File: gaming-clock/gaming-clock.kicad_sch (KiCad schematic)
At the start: 24 parts, among them J1 USB_C_Receptacle_USB2.0, U1 ESP32-C3-WROOM-02, U2 LM1117GS-3.3

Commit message: newsheet
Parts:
- removed D10, D11, D12, D13, D14, D15, D2, D3, D4, D5, D6, D7, D8, D9: SK6812MINI, LED_SMD:LED_SK6812MINI_PLCC4_3.5x3.5mm_P1.75mm, symbol LED:SK6812MINI
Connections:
- net 7-Segment-ARGB/DIN: now reaches U1.18 (GPIO0/ADC1_CH0/XTAL_32K_P)
- net DIN1 renamed 7-Segment-ARGB1/DIN
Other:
- added sheet 7-Segment-ARGB (untitled.kicad_sch)
- added sheet 7-Segment-ARGB1 (untitled.kicad_sch)

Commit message: c
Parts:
- removed D1: DＧＳ１０１０ＦＬ, Diode_SMD:D_SOD-123F, symbol Device:D
- added C5: 10u, Capacitor_SMD:C_0603_1608Metric_Pad1.08x0.95mm_HandSolder, symbol Device:C
- added C6: 100n, Capacitor_SMD:C_0603_1608Metric_Pad1.08x0.95mm_HandSolder, symbol Device:C
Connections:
- net +3.3V: now also C5.1, C6.1; no longer U1.1 (3V3)
- net 7-Segment-ARGB/DIN: now also U1.3 (GPIO4/ADC1_CH4); no longer U1.18 (GPIO0/ADC1_CH0/XTAL_32K_P)
- net 7-Segment-ARGB1/DIN: now also U1.4 (GPIO5/ADC2_CH0); no longer U1.17 (GPIO1/ADC1_CH1/XTAL_32K_N)
- net D-: now reaches U1.13 (GPIO18/USB_D-)
- net D-: now also J1.A7 (D-), J1.B7 (D-)
- net D+: now reaches U1.14 (GPIO19/USB_D+)
- net D+: now also J1.A6 (D+), J1.B6 (D+)
- net 7-Segment-ARGB2/DIN: now reaches U1.5 (GPIO6)
- net 7-Segment-ARGB3/DIN: now reaches U1.6 (GPIO7)
- new net: C5.2, C6.2, U1.1 (3V3)
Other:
- added sheet 7-Segment-ARGB2 (untitled.kicad_sch)
- added sheet 7-Segment-ARGB3 (untitled.kicad_sch)
- moved on the sheet: U1

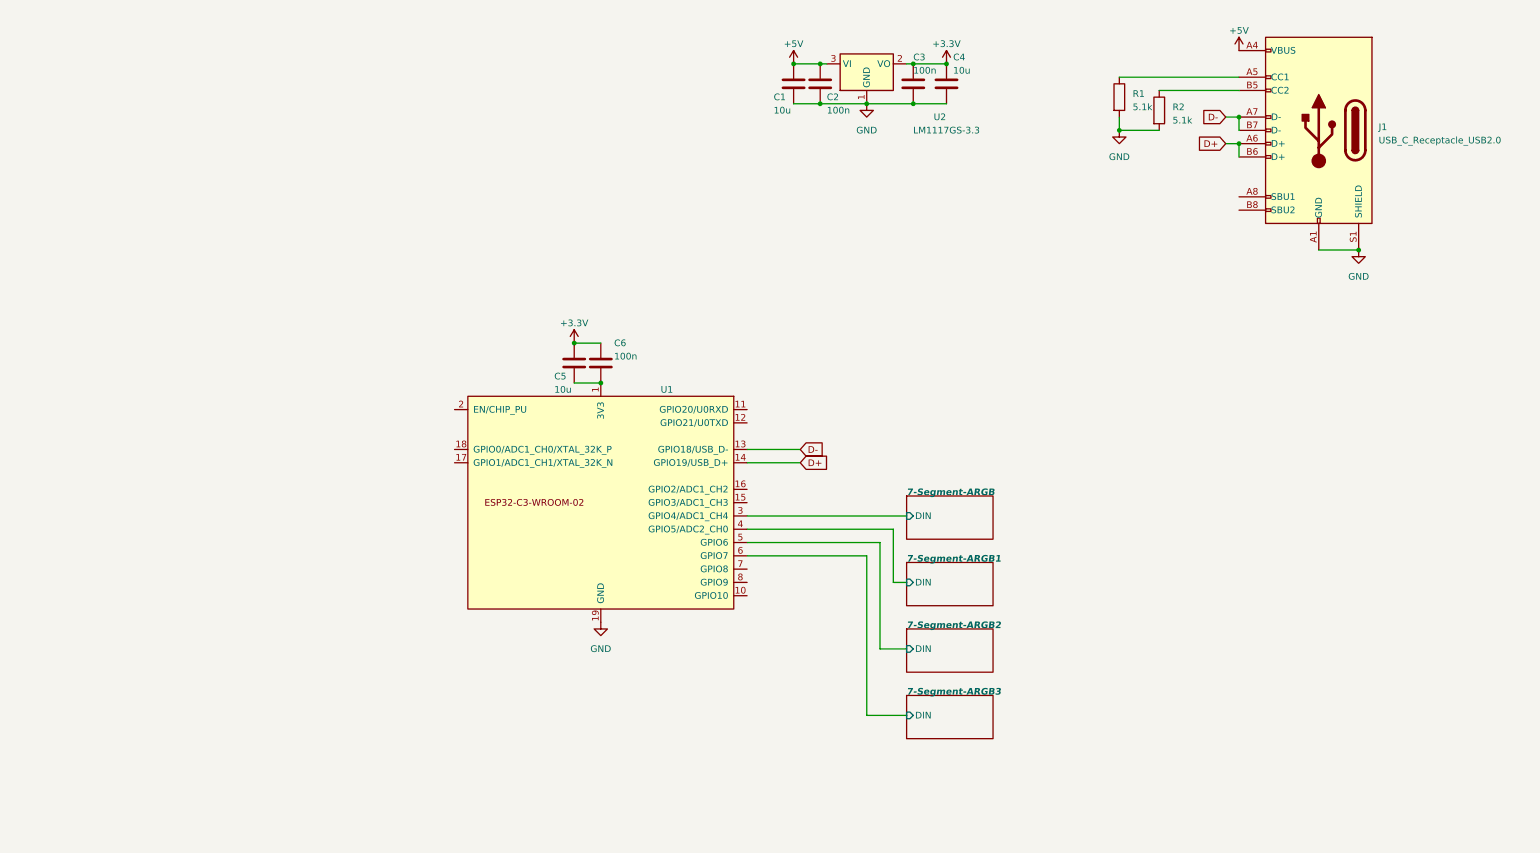
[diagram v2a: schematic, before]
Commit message: add dcjack
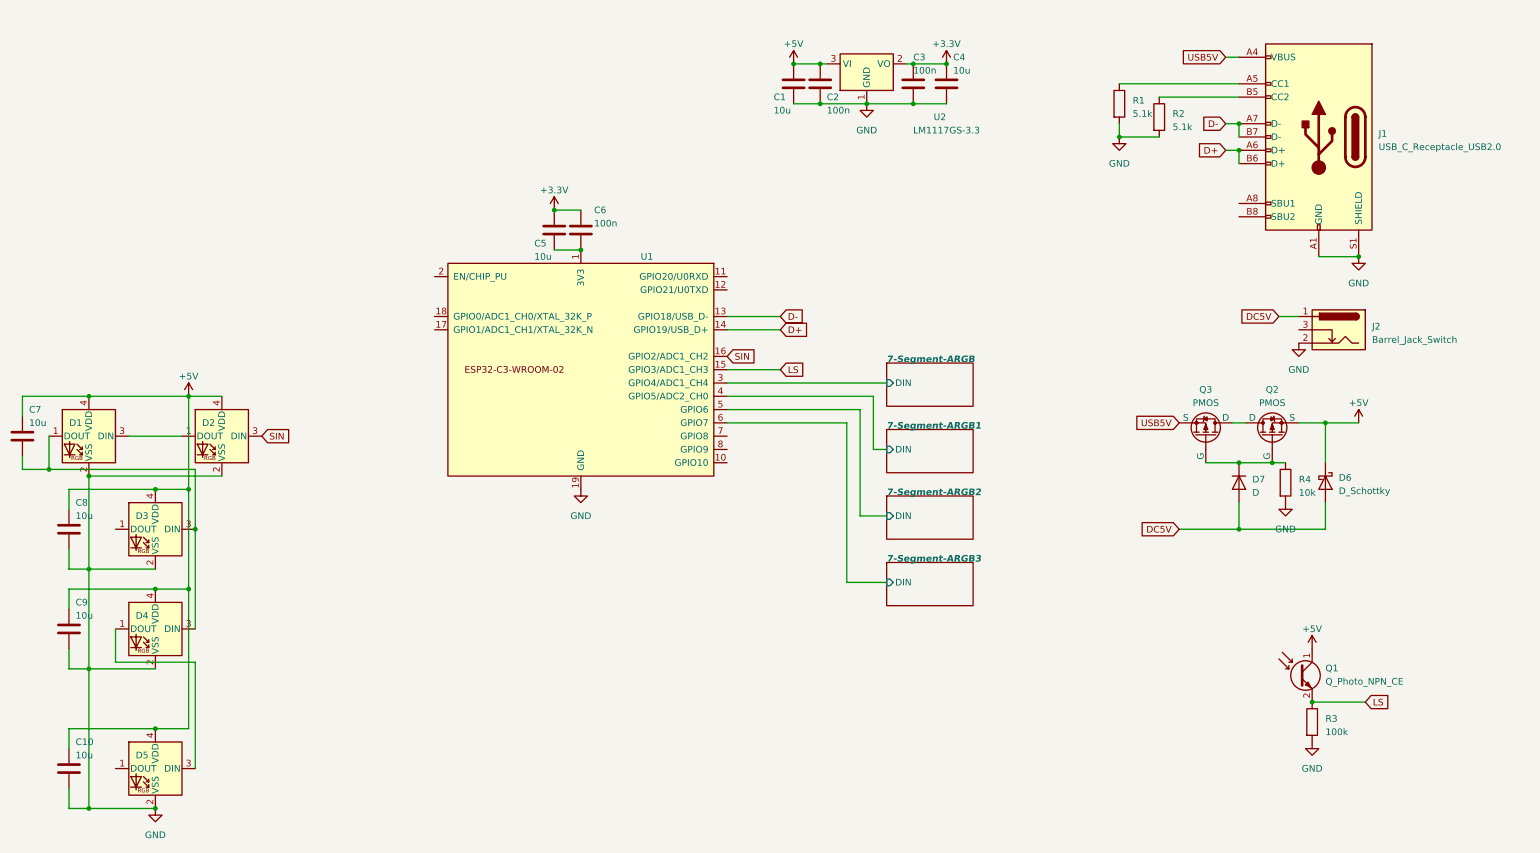
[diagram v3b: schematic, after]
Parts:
- added C10, C7, C8, C9: 10u, Capacitor_SMD:C_0603_1608Metric_Pad1.08x0.95mm_HandSolder, symbol Device:C
- added D1, D2, D3, D4, D5: SK6812MINI, LED_SMD:LED_SK6812MINI_PLCC4_3.5x3.5mm_P1.75mm, symbol LED:SK6812MINI
- added D6: D_Schottky, Diode_SMD:D_TUMD2, symbol Device:D_Schottky
- added D7: D, Diode_SMD:D_SOD-123, symbol Device:D
- added J2: Barrel_Jack_Switch, Lib:1.3mmDCjack, symbol Connector:Barrel_Jack_Switch
- added Q1: Q_Photo_NPN_CE, LED_THT:LED_D1.8mm_W1.8mm_H2.4mm_Horizontal_O3.81mm_Z1.6mm, symbol Device:Q_Photo_NPN_CE
- added Q2, Q3: PMOS, Package_TO_SOT_SMD:SOT-23, symbol Simulation_SPICE:PMOS
- added R3: 100k, Resistor_SMD:R_0603_1608Metric_Pad0.98x0.95mm_HandSolder, symbol Device:R
- added R4: 10k, Resistor_SMD:R_0603_1608Metric_Pad0.98x0.95mm_HandSolder, symbol Device:R
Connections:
- net +5V: now also C10.1, C7.1, C8.1, C9.1, D1.4 (VDD), D2.4 (VDD), D3.4 (VDD), D4.4 (VDD), D5.4 (VDD), D6.1 (K), Q1.1 (C), Q2.3 (S); no longer J1.A4 (VBUS), J1.A9 (VBUS), J1.B4 (VBUS), J1.B9 (VBUS)
- net GND: now also C10.2, C8.2, C9.2, D1.2 (VSS), D2.2 (VSS), D3.2 (VSS), D4.2 (VSS), D5.2 (VSS), J2.2, R3.2, R4.2
- net LS: now reaches U1.15 (GPIO3/ADC1_CH3)
- net LS: now also Q1.2 (E), R3.1
- net SIN: now reaches U1.16 (GPIO2/ADC1_CH2)
- net SIN: now also D2.3 (DIN)
- new net: D4.1 (DOUT), D5.3 (DIN)
- new net: D7.1 (K), Q2.2 (G), Q3.2 (G), R4.1
- new net: C7.2, D1.1 (DOUT), D3.3 (DIN), D4.3 (DIN)
- new net: D1.3 (DIN), D2.1 (DOUT)
- new net: Q2.1 (D), Q3.1 (D)
- new net DC5V: D6.2 (A), D7.2 (A), J2.1
- new net USB5V: J1.A4 (VBUS), J1.A9 (VBUS), J1.B4 (VBUS), J1.B9 (VBUS), Q3.3 (S)
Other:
- moved on the sheet: C5, C6, J1, R1, R2, U1

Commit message: fin
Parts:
- removed C5: 10u, Capacitor_SMD:C_0603_1608Metric_Pad1.08x0.95mm_HandSolder, symbol Device:C
- removed C6: 100n, Capacitor_SMD:C_0603_1608Metric_Pad1.08x0.95mm_HandSolder, symbol Device:C
- added LS101: Speaker, Buzzer_Beeper:Buzzer_TDK_PS1240P02BT_D12.2mm_H6.5mm, symbol Device:Speaker
- added R5, R6: 10k, Resistor_SMD:R_0603_1608Metric_Pad0.98x0.95mm_HandSolder, symbol Device:R
- added SW1: EN, Button_Switch_SMD:SW_Push_1P1T_NO_Vertical_Wuerth_434133025816, symbol Switch:SW_Push
- added SW2: BOOT, Button_Switch_SMD:SW_Push_1P1T_NO_Vertical_Wuerth_434133025816, symbol Switch:SW_Push
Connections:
- net +3.3V: now also U1.1 (3V3), R5.1, R6.1
- net 7-Segment-ARGB/DIN: now also U1.4 (GPIO5/ADC2_CH0); no longer U1.3 (GPIO4/ADC1_CH4)
- net 7-Segment-ARGB1/DIN: now also U1.3 (GPIO4/ADC1_CH4); no longer U1.4 (GPIO5/ADC2_CH0)
- net GND: now also C7.2, LS101.2, SW1.2, SW2.2
- net SPEAK: now reaches U1.18 (GPIO0/ADC1_CH0/XTAL_32K_P)
- net SPEAK: now also LS101.1
- net at U1.2 (EN/CHIP_PU): now also R5.2, SW1.1
- net GPIO8: now reaches U1.7 (GPIO8)
- net GPIO8: now also R6.2
- net GPIO9: now reaches U1.8 (GPIO9)
- net GPIO9: now also SW2.1
- net at D1.1 (DOUT), D3.3 (DIN), D4.3 (DIN): no longer C7.2

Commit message: pcb
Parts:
- removed D7: D, Diode_SMD:D_SOD-123, symbol Device:D
- removed J1: USB_C_Receptacle_USB2.0, Connector_USB:USB_C_Receptacle_G-Switch_GT-USB-7010ASV, symbol Connector:USB_C_Receptacle_USB2.0
- removed Q2, Q3: PMOS, Package_TO_SOT_SMD:SOT-23, symbol Simulation_SPICE:PMOS
- removed R4: 10k, Resistor_SMD:R_0603_1608Metric_Pad0.98x0.95mm_HandSolder, symbol Device:R
- added D7: D_Schottky, Diode_SMD:D_TUMD2, symbol Device:D_Schottky
- added J1: USB4145-03-0230-C, Lib:USB4145030230C, symbol USB4145-03-0230-C:USB4145-03-0230-C
- renumbered D2 to D1, D1 to D2
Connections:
- net 7-Segment-ARGB/DIN is gone; now on net 7-Segment-ARGB2/DIN: U1.4 (GPIO5/ADC2_CH0)
- net +5V: now also D7.1 (K)
- net 7-Segment-ARGB2/DIN: no longer U1.5 (GPIO6)
- net D+: now also J1.A6 (DP1), J1.B6 (DP2)
- net D-: now also J1.A7 (DN1), J1.B7 (DN2)
- net GND: now also J1.A1 (GND_1), J1.A12 (GND_2), J1.B1 (GND_3), J1.B12 (GND_4), J1.MH1 (MH5), J1.MH2 (MH6), J1.MH3, J1.MH4
- net USB5V: now also D7.2 (A), J1.A4 (VBUS_1), J1.A9 (VBUS_2), J1.B4 (VBUS_3), J1.B9 (VBUS_4)
- net at D3.1 (DOUT): now also D4.3 (DIN)
- net at D2.1 (DOUT), D3.3 (DIN): no longer D4.3 (DIN)
- net at R1.1: now also J1.A5 (CC1)
- net at R2.1: now also J1.B5 (CC2)
- new net 7-Segment-ARGB4/DIN: U1.5 (GPIO6)
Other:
- removed sheet 7-Segment-ARGB
- added sheet 7-Segment-ARGB4 (untitled.kicad_sch)
- moved on the sheet: D6, R1, R2
